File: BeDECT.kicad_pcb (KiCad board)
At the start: 4 copper layers, 60.6 x 24.1 mm, 28 parts, among them J1 EXP, J2 AudioJack3, SW1 SW_Push, U1 SC14CVMDECT

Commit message: update PCB
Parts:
- added LS1: Speaker, Connector_PinHeader_2.54mm:PinHeader_1x02_P2.54mm_Vertical, F.Cu at (170.3, 78.2)
- added REF**: MountingHole_2.1mm, MountingHole:MountingHole_2.1mm, F.Cu at (172.8, 75.8)
- added REF**: MountingHole_2.1mm, MountingHole:MountingHole_2.1mm, F.Cu at (170.2, 75.8)
- moved C7 5.50 mm to (166.2, 76.6)
- moved C6 5.34 mm to (166.2, 80.0)
- moved C9 5.27 mm to (167.9, 78.3)
- moved R10 3.13 mm to (122.2, 86.4), turned to 180 degrees
- moved SW1 3.12 mm to (167.5, 90.6)
- moved R8 2.03 mm to (163.5, 79.2)
- moved R9 2.03 mm to (163.5, 77.6)
- moved R3 1.83 mm to (174.8, 86.8)
- moved D2 1.63 mm to (176.1, 93.0)
- moved D1 1.43 mm to (176.1, 89.6)
- moved R4 1.30 mm to (139.2, 86.2)
- moved R2 0.85 mm to (173.3, 88.8)
- moved R1 0.81 mm to (162.5, 89.0)
- moved C2 0.20 mm to (135.7, 89.0)
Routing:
- net Net-(U1-LSRp): track 1.24 -> 24.5 mm, vias 1 -> 2
- net Net-(U1-LSRn): track 1.24 -> 24.2 mm, vias 1 -> 2
- net Net-(C6-Pad1): track 0.00 -> 9.43 mm
- net Net-(C7-Pad1): track 0.00 -> 6.46 mm
- net +3V3PI: track 81.0 -> 76.3 mm, vias 4 -> 5
- net Net-(R1-Pad1): track 2.51 -> 6.80 mm
- net Net-(U1-JTAG): track 6.94 -> 8.45 mm
- net Net-(D2-A): track 3.06 -> 3.96 mm
- net Net-(D2-K): track 19.4 -> 20.0 mm
- net GND: vias 4 -> 5

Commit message: update pcb
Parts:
- added SW2: SW_Push, beepis:1TS003A-1800-3500A-CT, F.Cu at (117.7, 91.3)
- added SW3: SW_Push, beepis:1TS003A-1800-3500A-CT, F.Cu at (117.7, 85.6)
- added SW4: SW_Push, beepis:1TS003A-1800-3500A-CT, F.Cu at (117.7, 80.0)
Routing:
- net /Pi_GPIO24: track 0.00 -> 48.4 mm, vias 0 -> 2
- net /Pi_GPIO23: track 0.00 -> 41.2 mm, vias 0 -> 2
- net /Pi_GPIO22: track 0.00 -> 34.0 mm, vias 0 -> 2
- net GND: vias 5 -> 4

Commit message: fix the funny on PCB
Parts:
- moved C4 2.32 mm to (133.6, 81.2), turned to 90 degrees
- moved C5 0.94 mm to (132.1, 79.7)
- moved R5 0.94 mm to (132.1, 82.9)
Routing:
- net Net-(C5-Pad2): track 19.2 -> 13.1 mm
- net Net-(U1-MICh): track 10.5 -> 6.06 mm
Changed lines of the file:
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@@
 	(footprint "Resistor_SMD:R_0603_1608Metric"
 		(layer "F.Cu")
-		(at 133 83.0375 90)
+		(at 132.075 82.9 90)
 		(descr "Resistor SMD 0603 (1608 Metric), square (rectangular) end terminal, IPC_7351 nominal, (Body size source: IPC-SM-782 page 72, https://www.pcb-3d.com/wordpress/wp-content/uploads/ipc-sm-782a_amendment_1_and_2.pdf), generated with kicad-footprint-generator")
 		(tags "resistor")
@@
 	(footprint "Capacitor_SMD:C_0603_1608Metric"
 		(layer "F.Cu")
-		(at 135.4 82.6 -45)
+		(at 133.575 81.175 90)
 		(descr "Capacitor SMD 0603 (1608 Metric), square (rectangular) end terminal, IPC_7351 nominal, (Body size source: IPC-SM-782 page 76, https://www.pcb-3d.com/wordpress/wp-content/uploads/ipc-sm-782a_amendment_1_and_2.pdf), generated with kicad-footprint-generator")
 		(tags "capacitor")
 		(property "Reference" "C4"
-			(at 2.545584 1.131371 180)
+			(at 2.545584 1.131371 135)
 			(layer "F.SilkS")
 			(hide yes)
@@
 		)
 		(property "Value" "33p"
-			(at 0 1.43 135)
+			(at 0 1.43 90)
 			(layer "F.Fab")
 			(hide yes)
@@
 		)
 		(property "Footprint" "Capacitor_SMD:C_0603_1608Metric"
-			(at 0 0 -45)
+			(at 0 0 90)
 			(unlocked yes)
 			(layer "F.Fab")
@@
 		)
 		(property "Datasheet" ""
-			(at 0 0 -45)
+			(at 0 0 90)
 			(unlocked yes)
 			(layer "F.Fab")
@@
 		)
 		(property "Description" "Unpolarized capacitor, small symbol"
-			(at 0 0 -45)
+			(at 0 0 90)
 			(unlocked yes)
 			(layer "F.Fab")
@@
 		(attr smd)
 		(fp_line
-			(start -0.140581 0.51)
-			(end 0.140581 0.51)
+			(start -0.140581 -0.51)
+			(end 0.140581 -0.51)
 			(stroke
 				(width 0.12)
@@
 		)
 		(fp_line
-			(start -0.140581 -0.51)
-			(end 0.140581 -0.51)
+			(start -0.140581 0.51)
+			(end 0.140581 0.51)
 			(stroke
 				(width 0.12)
@@
 		)
 		(fp_line
-			(start -1.48 0.73)
-			(end -1.48 -0.73)
+			(start 1.48 -0.73)
+			(end 1.48 0.73)
 			(stroke
 				(width 0.05)
@@
 		)
 		(fp_line
-			(start 1.48 -0.73)
-			(end 1.48 0.73)
+			(start -1.48 0.73)
+			(end -1.48 -0.73)
 			(stroke
 				(width 0.05)
@@
 		)
 		(fp_line
-			(start -0.8 0.4)
-			(end -0.8 -0.4)
+			(start 0.8 -0.4)
+			(end 0.8 0.4)
 			(stroke
 				(width 0.1)
@@
 		)
 		(fp_line
-			(start 0.8 -0.4)
-			(end 0.8 0.4)
+			(start -0.8 0.4)
+			(end -0.8 -0.4)
 			(stroke
 				(width 0.1)
@@
 		)
 		(fp_text user "${REFERENCE}"
-			(at 0 0 135)
+			(at 0 0 90)
 			(layer "F.Fab")
 			(effects
@@
 		)
 		(pad "1" smd roundrect
-			(at -0.775 0 315)
+			(at -0.775 0 90)
 			(size 0.9 0.95)
 			(layers "F.Cu" "F.Paste" "F.Mask")
@@
 		)
 		(pad "2" smd roundrect
-			(at 0.775 0 315)
+			(at 0.775 0 90)
 			(size 0.9 0.95)
 			(layers "F.Cu" "F.Paste" "F.Mask")
@@
 	(footprint "Capacitor_SMD:C_0603_1608Metric"
 		(layer "F.Cu")
-		(at 133 79.8125 90)
+		(at 132.075 79.675 90)
 		(descr "Capacitor SMD 0603 (1608 Metric), square (rectangular) end terminal, IPC_7351 nominal, (Body size source: IPC-SM-782 page 76, https://www.pcb-3d.com/wordpress/wp-content/uploads/ipc-sm-782a_amendment_1_and_2.pdf), generated with kicad-footprint-generator")
 		(tags "capacitor")
@@
 	)
 	(segment
-		(start 120 84.3)
-		(end 119.125001 84.3)
+		(start 152.04 95.19)
+		(end 152.04 96.5)
 		(width 0.2)
 		(layer "F.Cu")
@@
 	)
 	(segment
-		(start 152.04 95.24)
-		(end 151.6 94.8)
+		(start 151.55 94.7)
+		(end 152.04 95.19)
 		(width 0.2)
 		(layer "F.Cu")
@@
 	)
 	(segment
-		(start 152.04 96.5)
-		(end 152.04 95.24)
+		(start 120 84.3)
+		(end 119.125001 84.3)
 		(width 0.2)
 		(layer "F.Cu")
@@
 	)
 	(via
-		(at 151.6 94.8)
+		(at 151.55 94.7)
 		(size 0.6)
 		(drill 0.3)
@@
 	)
 	(segment
-		(start 149.6 92.8)
-		(end 151.6 94.8)
+		(start 120 88.5)
+		(end 120 84.3)
 		(width 0.2)
 		(layer "B.Cu")
@@
 	(segment
 		(start 124.3 92.8)
-		(end 149.6 92.8)
+		(end 120 88.5)
 		(width 0.2)
 		(layer "B.Cu")
@@
 	)
 	(segment
-		(start 120 88.5)
+		(start 149.65 92.8)
 		(end 124.3 92.8)
 		(width 0.2)
@@
 	)
 	(segment
-		(start 120 84.3)
-		(end 120 88.5)
+		(start 151.55 94.7)
+		(end 149.65 92.8)
 		(width 0.2)
 		(layer "B.Cu")
@@
 	)
 	(segment
-		(start 154.58 96.5)
-		(end 154.58 95.48)
+		(start 153.85 94.7)
+		(end 154.58 95.43)
 		(width 0.2)
 		(layer "F.Cu")
@@
 	)
 	(segment
-		(start 154.58 95.48)
-		(end 153.9 94.8)
+		(start 154.58 95.43)
+		(end 154.58 96.5)
 		(width 0.2)
 		(layer "F.Cu")
@@
 	)
 	(via
-		(at 153.9 94.8)
+		(at 153.85 94.7)
 		(size 0.6)
 		(drill 0.3)
@@
 	)
 	(segment
-		(start 153.9 94.8)
-		(end 151.5 92.4)
+		(start 120.6 87.7)
+		(end 120.6 79.3)
 		(width 0.2)
 		(layer "B.Cu")
@@
 	)
 	(segment
-		(start 120.6 87.7)
-		(end 120.6 79.3)
+		(start 151.5 92.4)
+		(end 125.3 92.4)
 		(width 0.2)
 		(layer "B.Cu")
@@
 	)
 	(segment
-		(start 125.3 92.4)
-		(end 120.6 87.7)
+		(start 153.85 94.7)
+		(end 153.8 94.7)
 		(width 0.2)
 		(layer "B.Cu")
@@
 	)
 	(segment
-		(start 151.5 92.4)
-		(end 125.3 92.4)
+		(start 125.3 92.4)
+		(end 120.6 87.7)
+		(width 0.2)
+		(layer "B.Cu")
+		(net 8)
+	)
+	(segment
+		(start 153.8 94.7)
+		(end 151.5 92.4)
 		(width 0.2)
 		(layer "B.Cu")
@@
 	)
 	(segment
-		(start 136.1125 80.75)
-		(end 133 83.8625)
-		(width 0.2)
-		(layer "F.Cu")
-		(net 31)
-	)
-	(segment
 		(start 137.95 77.15)
 		(end 140.05 79.25)
@@
 	)
 	(segment
-		(start 130.6375 79.0375)
-		(end 130.05 78.45)
-		(width 0.2)
-		(layer "F.Cu")
-		(net 70)
-	)
-	(segment
 		(start 131 75.5)
 		(end 130.05 75.5)
@@
 	)
 	(segment
-		(start 133 79.0375)
-		(end 130.6375 79.0375)
-		(width 0.2)
-		(layer "F.Cu")
-		(net 70)
-	)
-	(segment
 		(start 130.05 75.5)
 		(end 121.95 75.5)
@@
 	)
 	(segment
-		(start 130.05 78.45)
-		(end 130.05 75.5)
-		(width 0.2)
-		(layer "F.Cu")
-		(net 70)
-	)
-	(segment
 		(start 135.05 75.5)
 		(end 131 75.5)
@@
 	)
 	(segment
-		(start 133 82.2125)
-		(end 133 80.5875)
+		(start 132.075 82.075)
+		(end 132.075 80.45)
 		(width 0.2)
 		(layer "F.Cu")

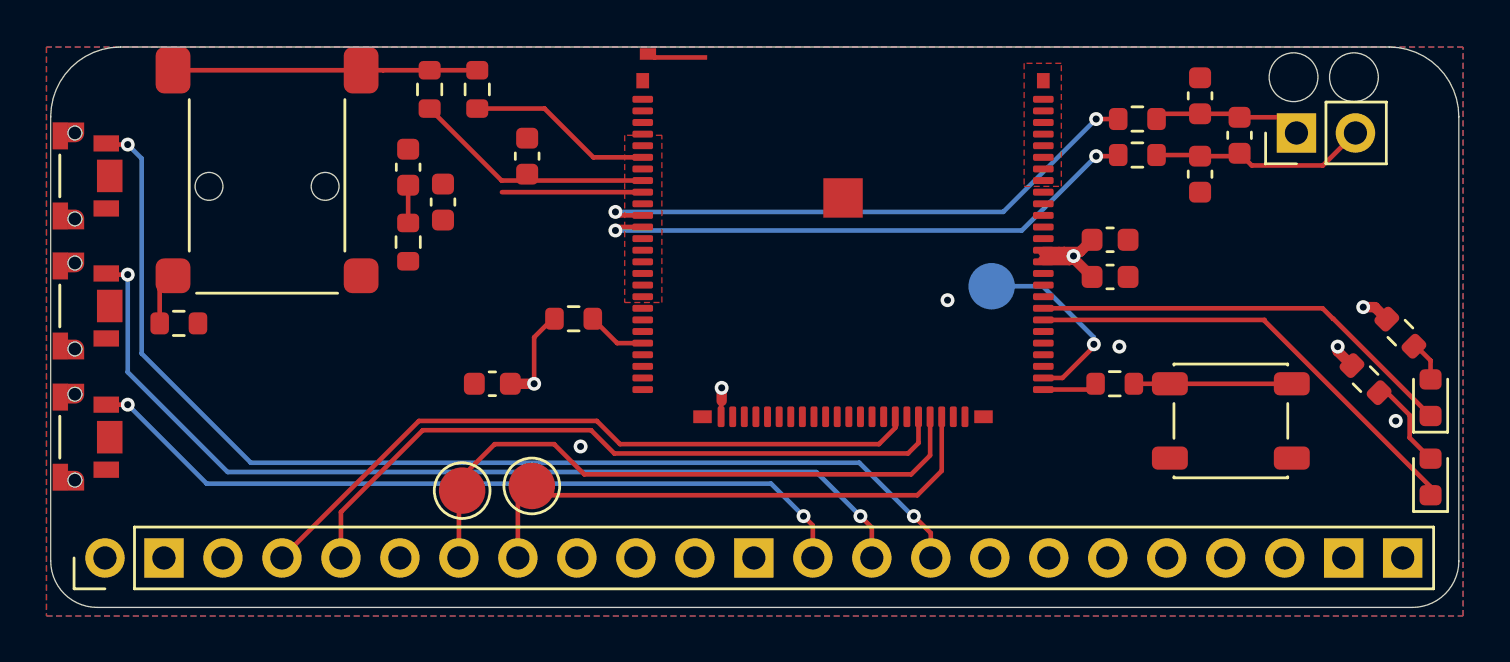
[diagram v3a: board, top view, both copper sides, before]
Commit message: Update PCB: Add button pullups
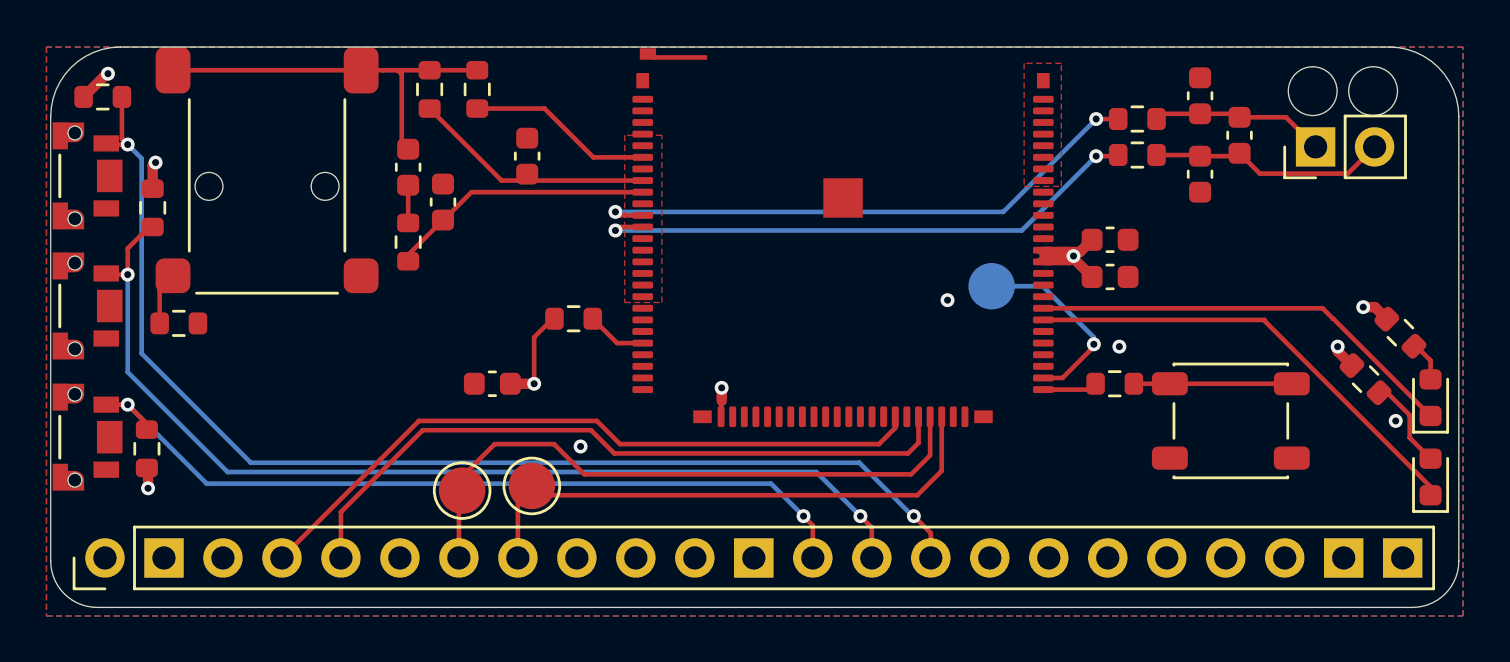
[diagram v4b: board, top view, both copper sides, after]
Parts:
- added R11: 5K1, Resistor_SMD:R_0603_1608Metric, F.Cu at (120.8, 91.8)
- added R12: 5K1, Resistor_SMD:R_0603_1608Metric, F.Cu at (118.9, 76.7)
- added R13: 5K1, Resistor_SMD:R_0603_1608Metric, F.Cu at (121.1, 81.4)
- moved REF** 1.02 mm to (171.0, 76.4)
- moved LS1 1.02 mm to (171.2, 78.8)
- moved REF** 1.02 mm to (173.6, 76.4)
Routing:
- net +3V3PI: track 76.5 -> 104.0 mm, vias 5 -> 8
- net Net-(U1-MICh): track 6.06 -> 11.5 mm
- net Net-(C5-Pad2): track 13.1 -> 16.7 mm
- net /Pi_GPIO23: track 41.3 -> 43.8 mm
- net /Pi_GPIO24: track 48.4 -> 50.6 mm
- net /Pi_GPIO22: track 34.0 -> 35.4 mm
- net Net-(C7-Pad1): track 6.46 -> 7.53 mm
- net Net-(C6-Pad1): track 9.43 -> 10.3 mm

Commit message: Update PCB: via stitching, silkscreen
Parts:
- added G***: LOGO, LOGO, F.Cu at (169.3, 82.7)
- added G***: LOGO, LOGO, F.Cu at (174.5, 82.1)
- added TP4: TestPoint, TestPoint:TestPoint_Pad_D1.0mm, F.Cu at (131.5, 92.6)
- moved TP2 0.22 mm to (134.3, 93.4)
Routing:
- net /Pi_SCL: track 30.0 -> 31.5 mm
- net /Pi_SDA: track 30.0 -> 31.3 mm
- net +3V3PI: track 104.0 -> 103.4 mm
- net GND: vias 4 -> 51
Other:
- board text added: "RX"
- board text added: "TX"
- board text added: "trans rights"

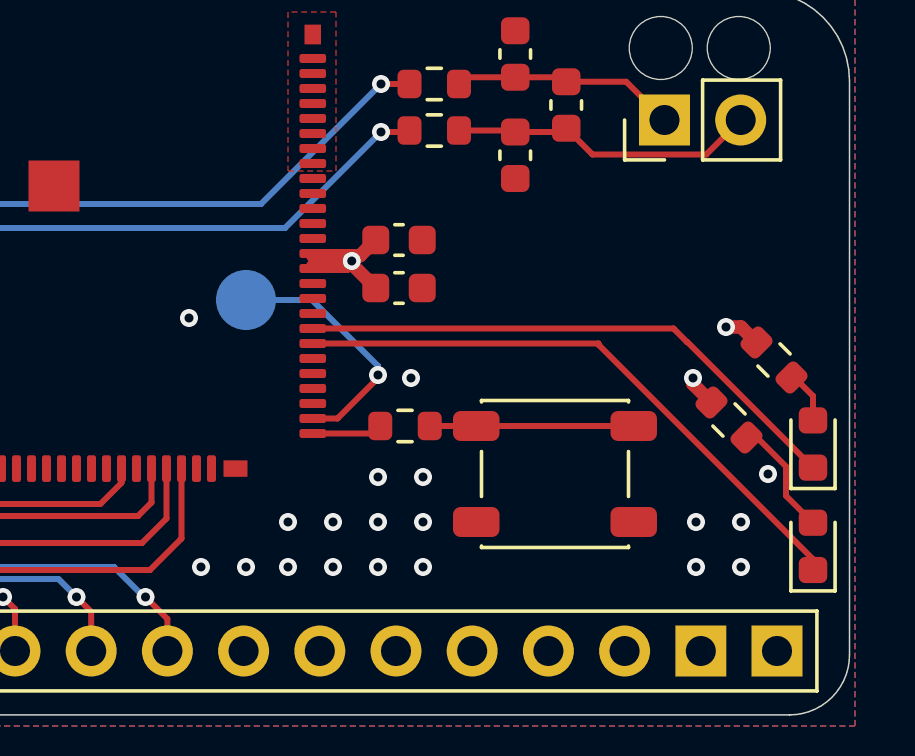
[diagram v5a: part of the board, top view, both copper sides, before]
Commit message: Update PCB: via stitching, silkscreen
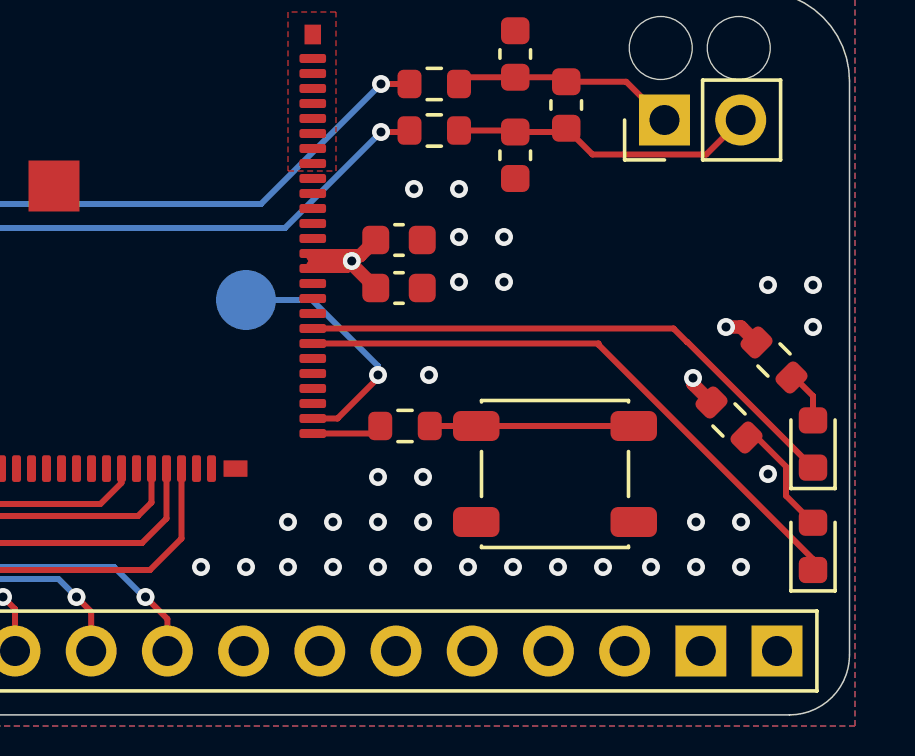
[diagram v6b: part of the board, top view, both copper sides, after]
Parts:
- added G***: LOGO, LOGO, B.Cu at (152.4, 79.0)
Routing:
- net GND: vias 51 -> 64
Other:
- board text added: "BeDECT v0.1 by Treble"
